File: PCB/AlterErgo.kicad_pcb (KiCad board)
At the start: 2 copper layers, 106 parts, among them J1 GS3, J2 SJ-43514, J3 GS3, J4 Conn_01x02, SW0:10 SW_Push, SW0:11 SW_Push, SW0:12 SW_Push, SW0:7 SW_Push, SW0:8 SW_Push, SW0:9 SW_Push, SW1 SW_SPST, SW1:10 SW_Push, SW1:11 SW_Push, SW1:12 SW_Push, SW1:13 SW_Push, SW1:7 SW_Push, SW1:8 SW_Push, SW1:9 SW_Push, SW2:10 SW_Push, SW2:11 SW_Push, SW2:12 SW_Push, SW2:13 SW_Push, SW2:7 SW_Push, SW2:8 SW_Push, SW2:9 SW_Push, SW3:10 SW_Push, SW3:11 SW_Push, SW3:12 SW_Push, SW3:13 SW_Push, SW3:8 SW_Push, SW3:9 SW_Push, SW4:10 SW_Push, SW4:11 SW_Push, SW4:12 SW_Push, SW4:13 SW_Push, SW4:7 SW_Push, SW4:8 SW_Push, SW4:9 SW_Push, SW5:10 SW_Push, SW5:11 SW_Push, SW5:12 SW_Push, SW5:13 SW_Push, SW5:7 SW_Push, SW5:8 SW_Push, SW5:9 SW_Push, U1 Feather32u4Bluefruit, U2 MCP23018

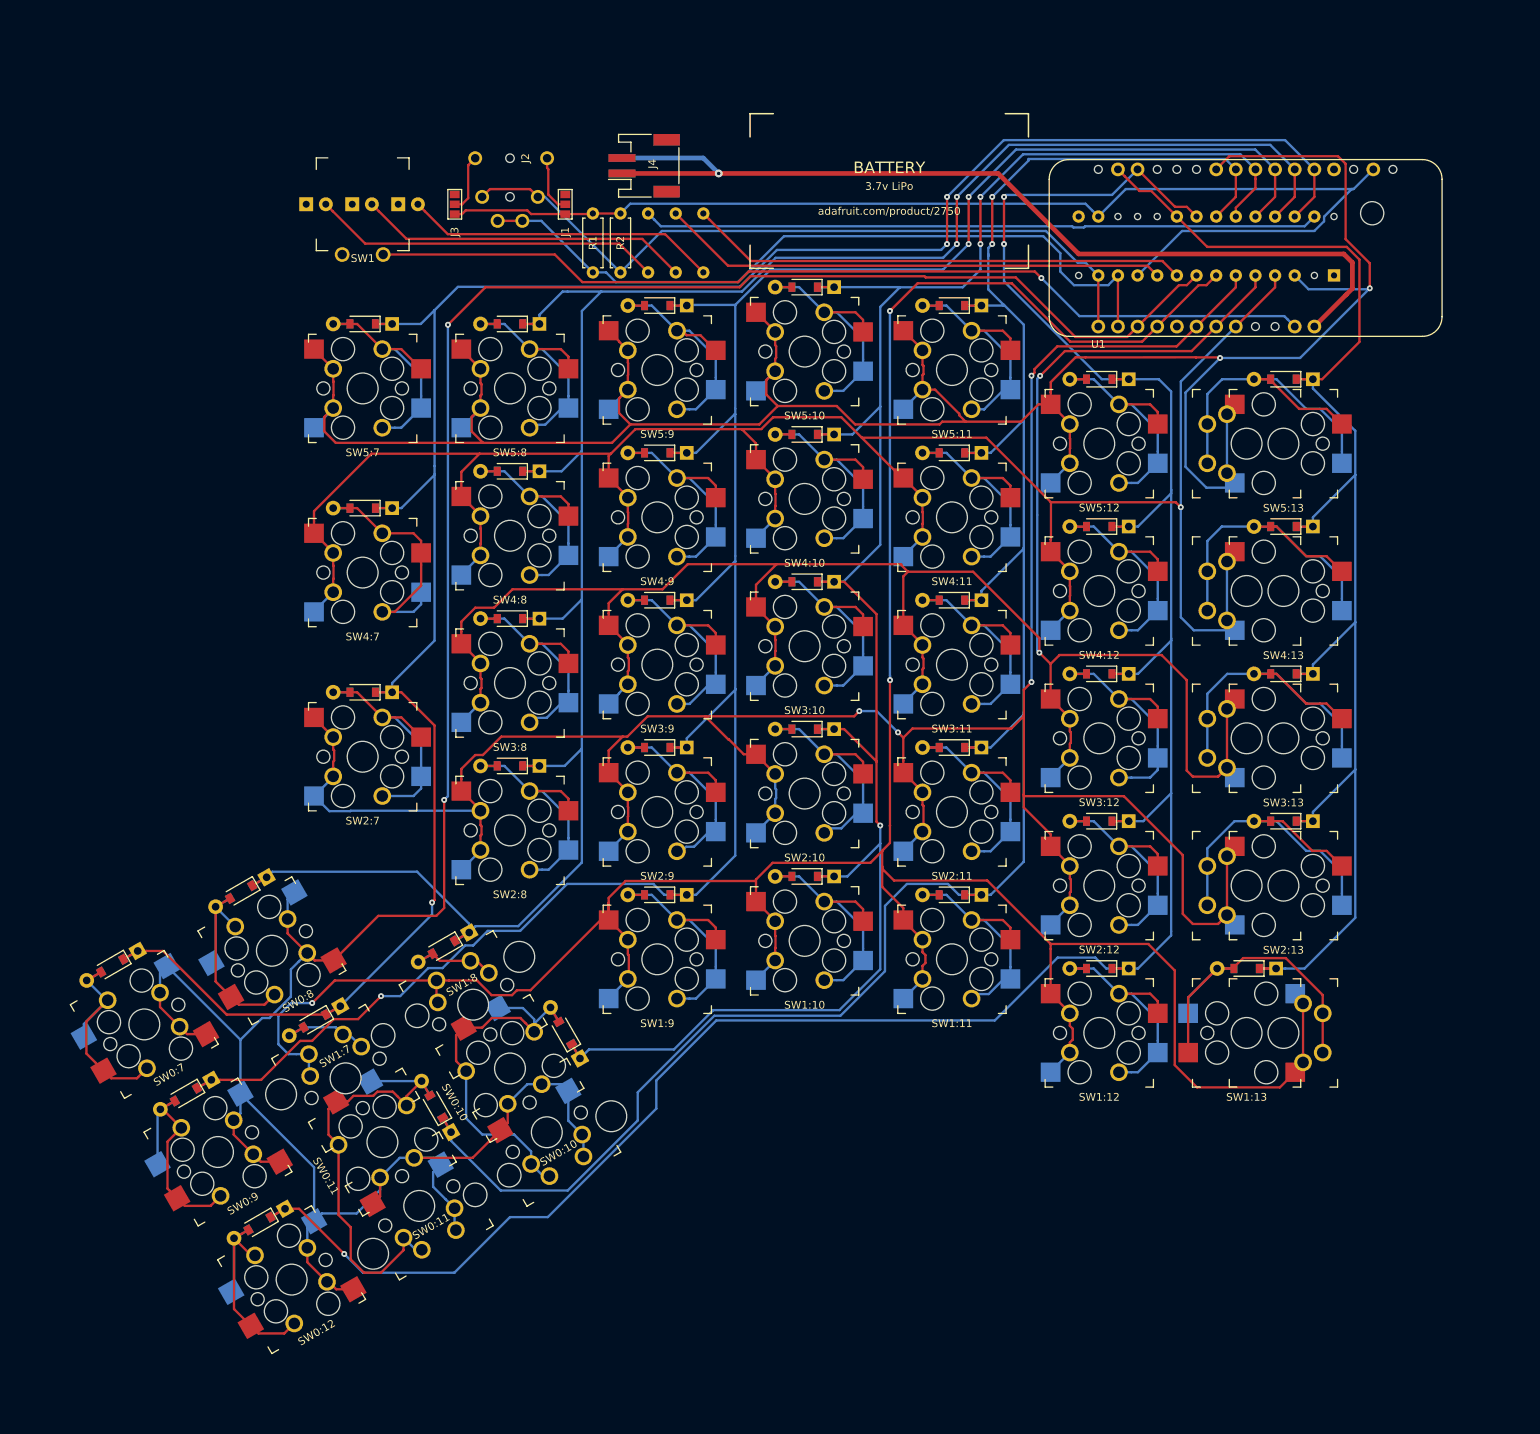
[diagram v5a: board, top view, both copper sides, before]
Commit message: Add board outline; adjust position of components; adjust routing of some traces; add ground planes; add OSHW logo
SW1 (power toggle) was moved down to match the key spacing. TRRS jack was moved up to match the edge of the board. The traces that were moved were moved in order to allow better ground plane fill and clean up some around the thumb cluster.
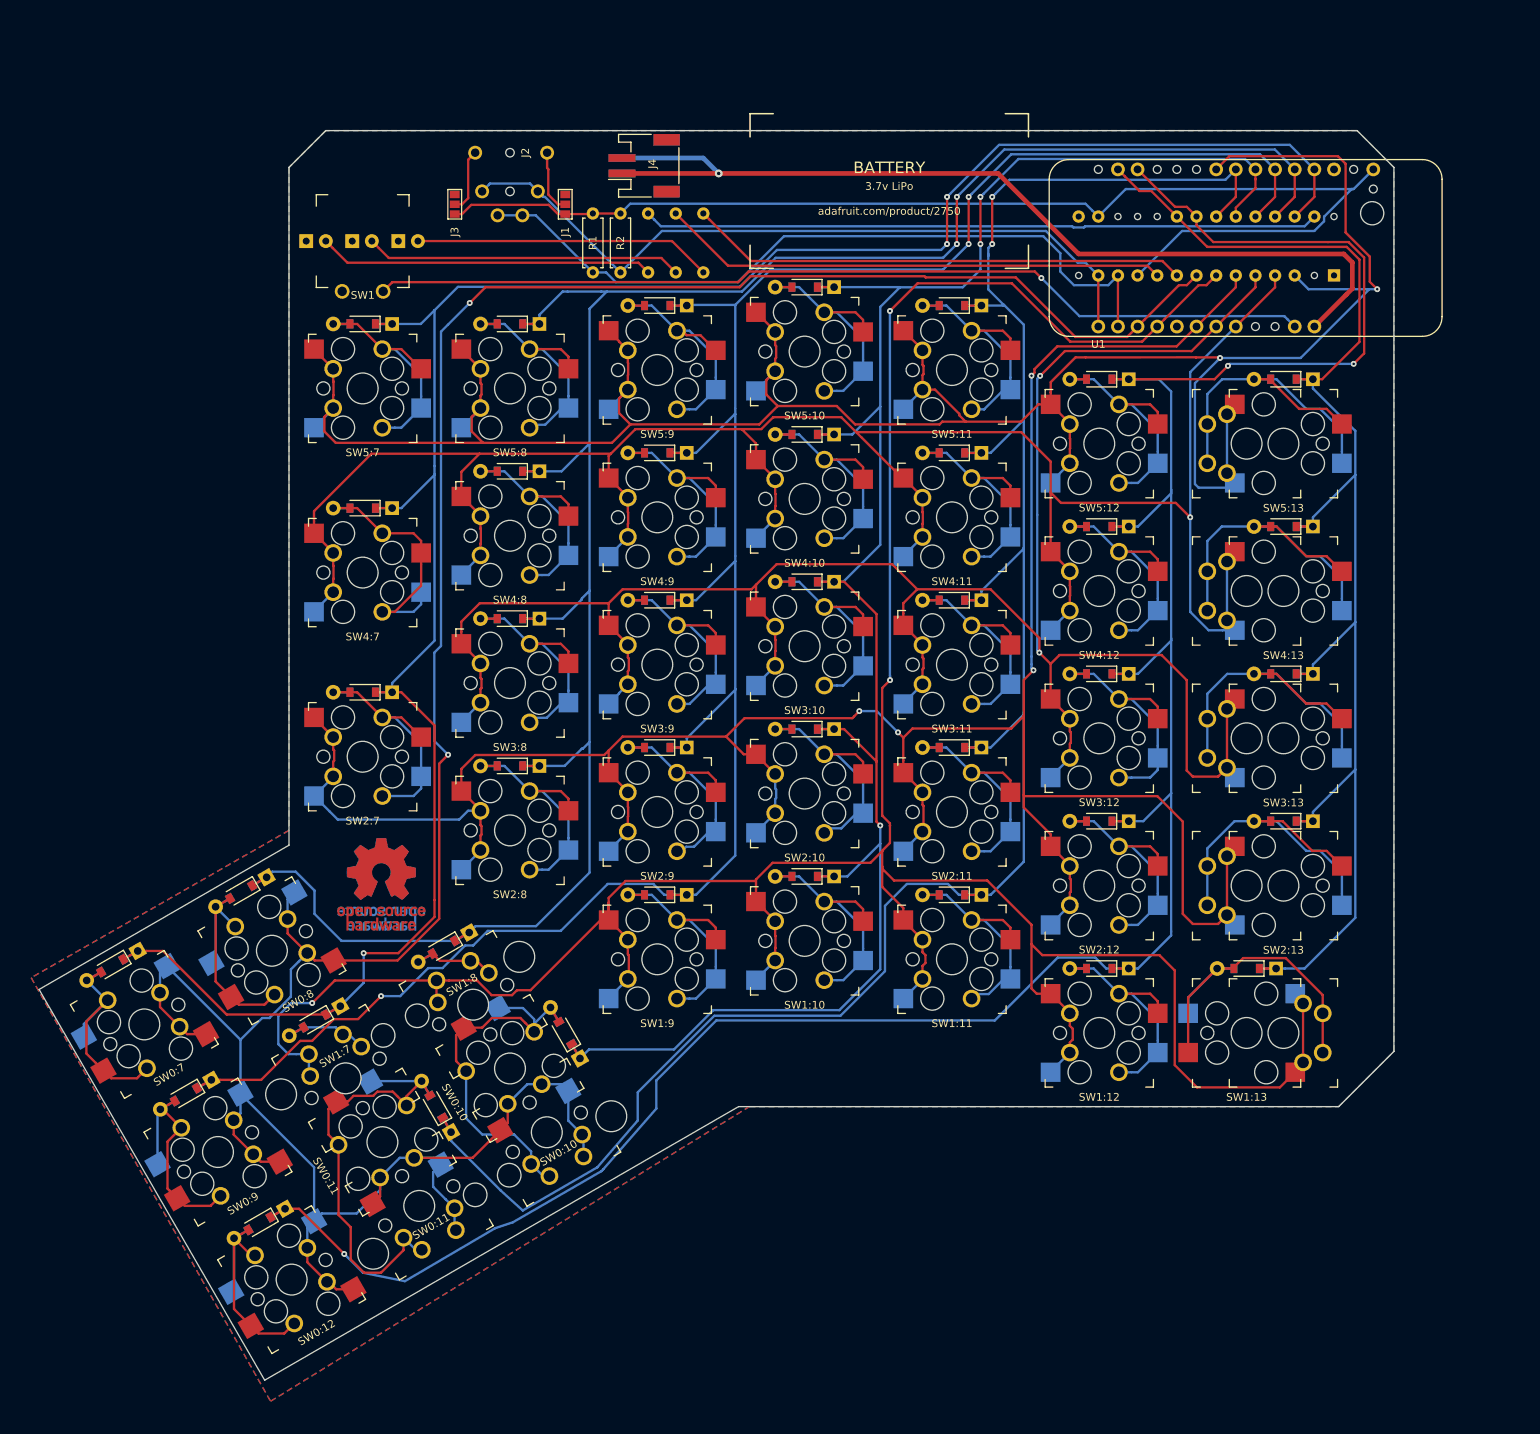
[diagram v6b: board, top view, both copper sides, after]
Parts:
- added REF***: OSHW-Logo_11.4x12mm_Copper, Symbols:OSHW-Logo_11.4x12mm_Copper, B.Cu at (83.4, 121.3)
- added REF***: OSHW-Logo_11.4x12mm_Copper, Symbols:OSHW-Logo_11.4x12mm_Copper, F.Cu at (83.4, 121.3)
- moved D1 4.76 mm to (85.6, 38.1)
- moved D2 4.76 mm to (79.6, 38.1)
- moved D3 4.76 mm to (73.7, 38.1)
- moved SW1 4.76 mm to (81.0, 38.1)
- moved J2 0.71 mm to (100.0, 26.7)
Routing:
- net /COL1: track 321.4 -> 340.0 mm
- net /ROW3: track 292.3 -> 284.1 mm
- net /COL5: track 289.5 -> 294.6 mm
- net /ROW1: track 379.7 -> 384.0 mm
- net /ROW4: track 294.9 -> 299.1 mm
- net /ROW2: track 341.1 -> 338.4 mm
- net /COL6: track 298.6 -> 300.7 mm
- net Net-(D3-Pad2): track 45.3 -> 43.3 mm
- net Net-(D2-Pad2): track 42.9 -> 41.0 mm
- net Net-(D1-Pad2): track 40.6 -> 38.6 mm
- net /ROW0: track 377.1 -> 379.0 mm
- net /ROW5: track 329.3 -> 330.4 mm
- net Net-(SW1-Pad2): track 122.9 -> 121.9 mm
- net Net-(J2-Pad4): track 7.60 -> 8.32 mm
- net Net-(J1-Pad2): track 7.47 -> 8.19 mm
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- added copper zone on B.Cu, net GND
- added copper zone on F.Cu, net GND
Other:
- board outline added: 175.2 x 161.6 mm

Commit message: Remove separate battery connector points; position Feather underneath the PCB
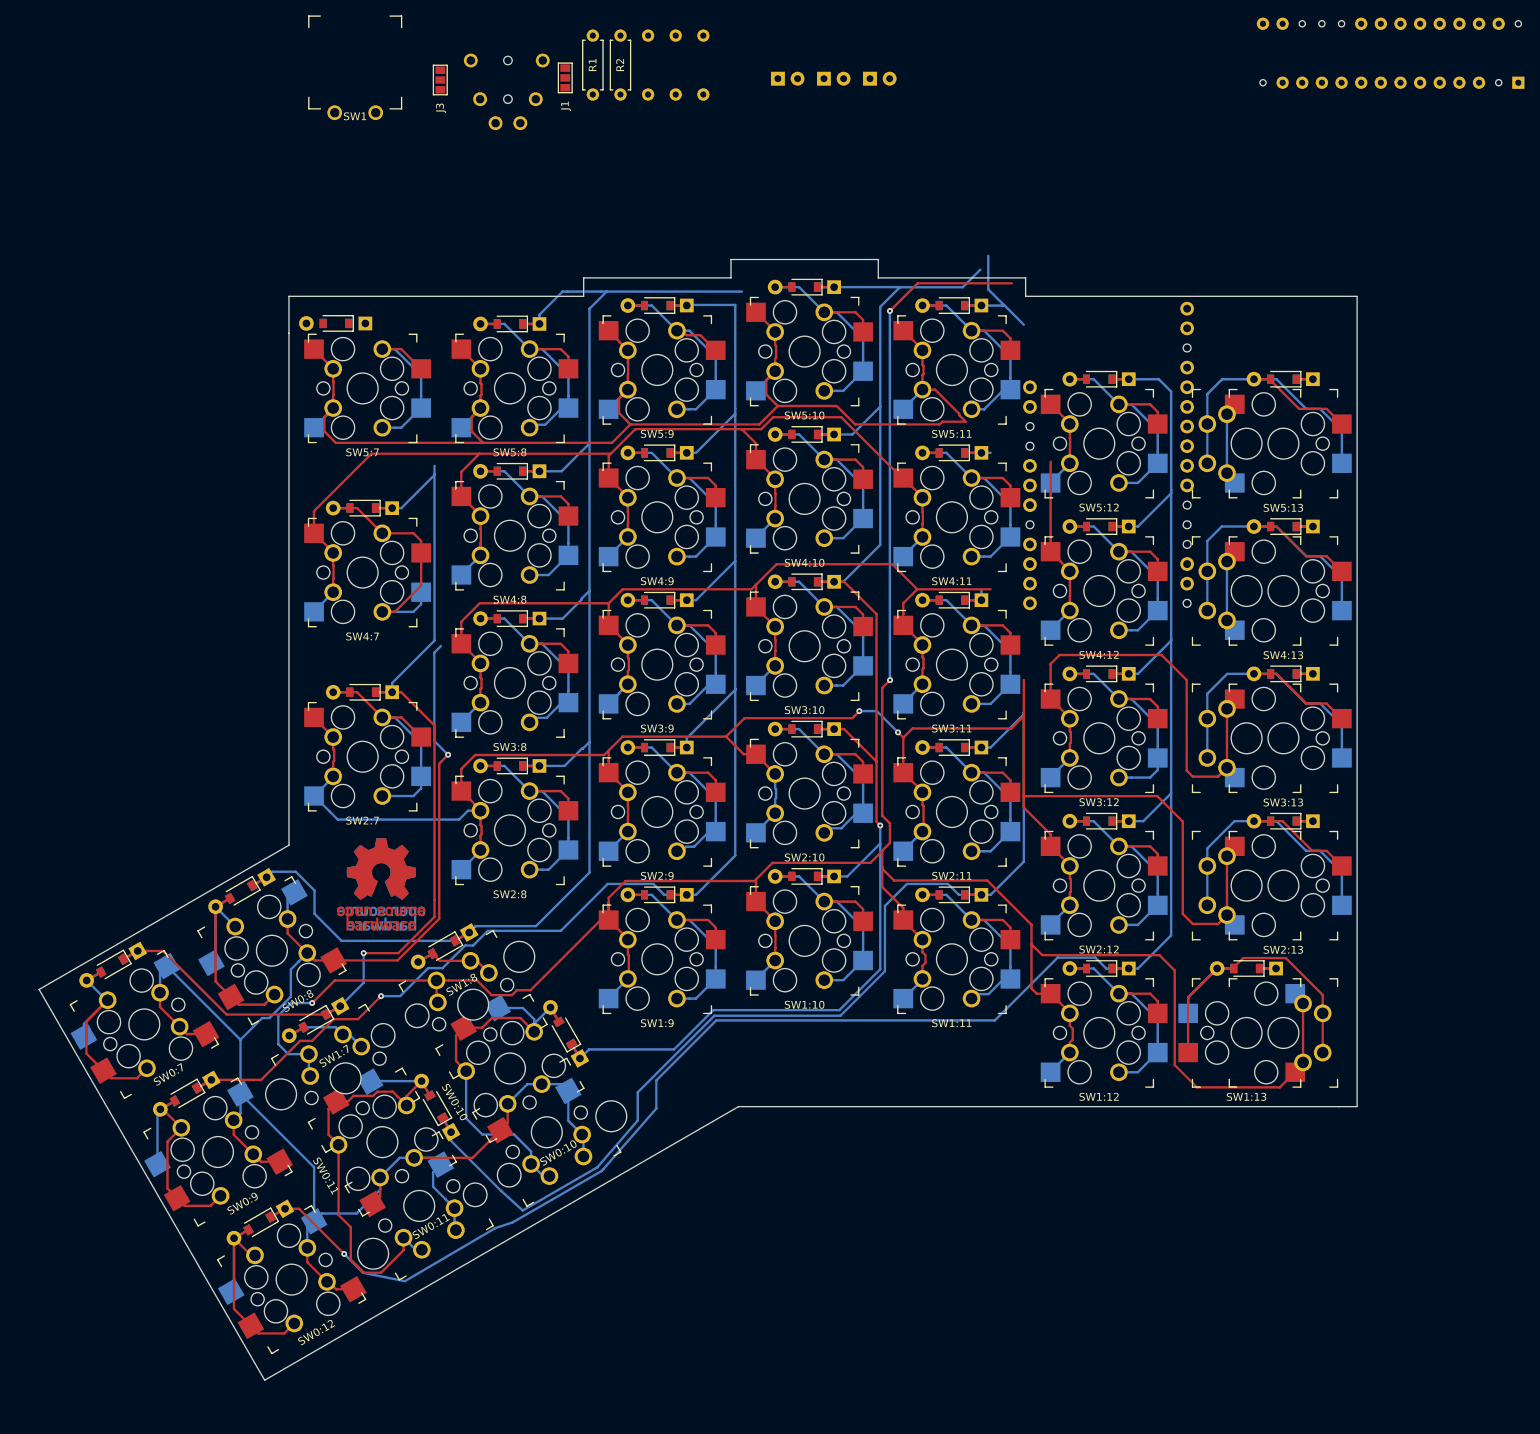
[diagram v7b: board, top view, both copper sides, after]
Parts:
- removed J4 (x2): Conn_01x02, Connectors_JST:JST_PH_S2B-PH-SM4-TB_02x2.00mm_Angled
- removed RESET: ResetHole, Mounting_Holes:MountingHole_3mm
- J2, U1: moved to B.Cu
- moved D1 64.5 mm to (146.6, 17.1)
- moved D2 64.5 mm to (140.6, 17.1)
- moved D3 64.5 mm to (134.7, 17.1)
- moved U2 34.5 mm to (230.4, 17.6)
- moved U1 32.2 mm to (177.4, 65.9), turned to 270 degrees
- moved SW1 23.1 mm to (80.0, 15.0)
- moved R1 23.0 mm to (110.7, 11.5)
- moved R2 23.0 mm to (114.3, 11.5)
- moved R3 23.0 mm to (125.0, 19.1)
- moved R4 23.0 mm to (121.4, 19.1)
- moved R5 23.0 mm to (117.9, 19.1)
- moved J1 16.3 mm to (107.2, 17.0)
- moved J3 16.2 mm to (91.0, 17.3)
- moved J2 11.9 mm to (99.8, 14.8)
- moved D5:7 3.46 mm to (77.5, 48.8)
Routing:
- net /COL0: track 188.4 -> 21.9 mm
- net /COL6: track 300.7 -> 135.3 mm, vias 3 -> 1
- net +3V3: track 156.3 -> 0.00 mm
- net /ROW0: track 379.0 -> 231.2 mm, vias 2 -> 1
- net /ROW5: track 330.4 -> 199.0 mm, vias 2 -> 0
- net Net-(J4-Pad1): track 122.8 -> 0.00 mm, vias 1 -> 0
- net Net-(SW1-Pad2): track 121.9 -> 0.00 mm, vias 1 -> 0
- net /COL11: track 284.7 -> 172.5 mm, vias 2 -> 0
- net /ROW4: track 299.1 -> 198.2 mm, vias 1 -> 0
- net /SCL: track 97.4 -> 0.00 mm
- net /SDA: track 96.1 -> 0.00 mm
- net /COL5: track 294.6 -> 203.7 mm, vias 2 -> 0
- net /COL4: track 299.0 -> 209.6 mm, vias 3 -> 1
- net Net-(R5-Pad2): track 87.5 -> 0.00 mm
- net /ROW3: track 284.1 -> 201.1 mm, vias 2 -> 0
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- removed copper zone on B.Cu, net GND
- removed copper zone on F.Cu, net GND
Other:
- board size 175.2 x 161.6 mm -> 170.4 x 144.9 mm
- board text removed: "3.7v LiPo adafruit.com/product/2750"
- board text removed: "BATTERY"
